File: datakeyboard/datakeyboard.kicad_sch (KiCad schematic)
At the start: 22 parts, among them U1 PIC24FJ128GB204

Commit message: Power supply
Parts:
- removed C?: 100nF, symbol Device:C_Small
- removed R?: R_Small, symbol Device:R_Small
- removed R?: 100, symbol Device:R_Small
- removed U?: FS8205A, symbol Library:FS8205A
- removed U?: DW01A, symbol Library:DW01A
- added C?: 10uF, symbol Device:C_Small
- added D? (x2): LED, symbol Device:LED
- added F?: 400mA, symbol Device:Fuse
- added J?: Micro_SD_Card, symbol Connector:Micro_SD_Card
- added R? (x2): 1k, symbol Device:R_Small
- U?: value AMS1117-3.3 -> AMS1117-3.0
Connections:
- net B- is gone; now on net GND: JBAT.2 (Pin_2)
- net GND: now also C?.1, C?.2; no longer C?.2
- net RESET: now also R?.2; no longer R?.1
- net VUSB: now also F?.2; no longer C?.1, U?.4 (VCC), U?.8 (CE)
- net at C?.1, R?.2: now also R?.1; no longer R?.2
- net at U?.6 (STDBY): now also R?.2
- net at U?.7 (CHRG): now also R?.2
- net +3.3V renamed +3V0
- net VBAT: no longer names the net of JBAT.1 (Pin_1), U?.3 (VI), U?.5 (BAT)
- net VBAT: now also C?.1
- new net: C?.2, D?.2 (A), D?.2 (A), F?.1, U?.4 (VCC), U?.8 (CE)
- new net: D?.1 (K), R?.1 (x2)
- no-connect marks 7 -> 2
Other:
- note removed: "CHARGING"
- note removed: "PROTECTION"
- moved on the sheet: C?, R?, U?

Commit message: Display light
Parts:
- added JDISP: Conn_01x08, symbol Connector_Generic:Conn_01x08
- added Q? (x2): BSS83P, Package_TO_SOT_SMD:SOT-23, symbol Transistor_FET:BSS83P
- added SW0, SW1, SW2, SW3, SW4, SW5: SW_Push, symbol Switch:SW_Push
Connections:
- net +3V0: now also Q?.2 (S), Q?.2 (S)
- net GND: now also J?.6 (VSS), JDISP.1 (Pin_1), SW0.1, SW1.1, SW2.1, SW3.1, SW4.1, SW5.1
- net VIO: now reaches J?.4 (VDD)
- net VIO: now also JDISP.2 (Pin_2), Q?.3 (D)
- net SCLK: now reaches U1.1 (RB9)
- net SCLK: now also JDISP.3 (Pin_3)
- net RES_D: now reaches U1.11 (RB13)
- net RES_D: now also JDISP.5 (Pin_5)
- net at U1.23 (RB2): now also Q?.1 (G)
- net MOSI: now reaches U1.3 (RC7)
- net MOSI: now also JDISP.4 (Pin_4)
- net BTN0: now reaches U1.32 (RA8)
- net BTN0: now also SW0.2
- net BTN1: now reaches U1.33 (RB4)
- net BTN1: now also SW1.2
- net CS_D: now reaches U1.4 (RC8)
- net CS_D: now also JDISP.7 (Pin_7)
- net RS_D: now reaches U1.5 (PC9)
- net RS_D: now also JDISP.6 (Pin_6)
- new net BNT3: SW3.2
- new net BTN2: SW2.2
- new net BTN4: SW4.2
- new net BTN5: SW5.2
- new net LEDA: JDISP.8 (Pin_8), Q?.3 (D)
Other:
- moved on the sheet: C?, J?

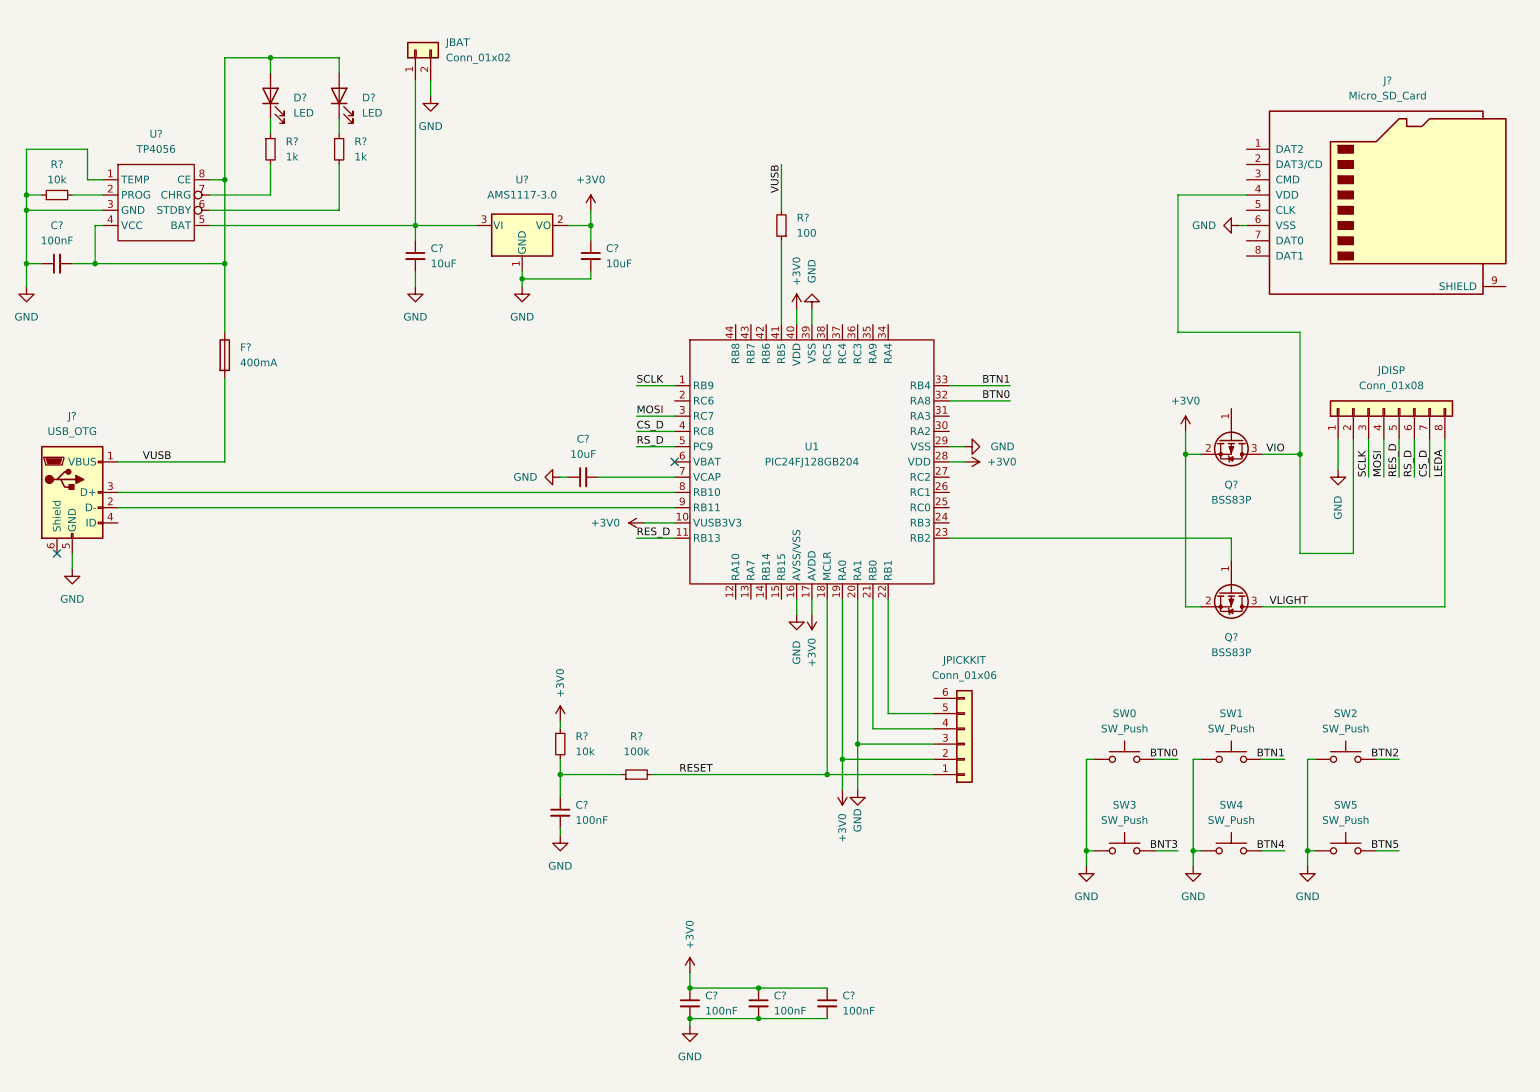
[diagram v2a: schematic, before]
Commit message: Wire up SDCard and buttons
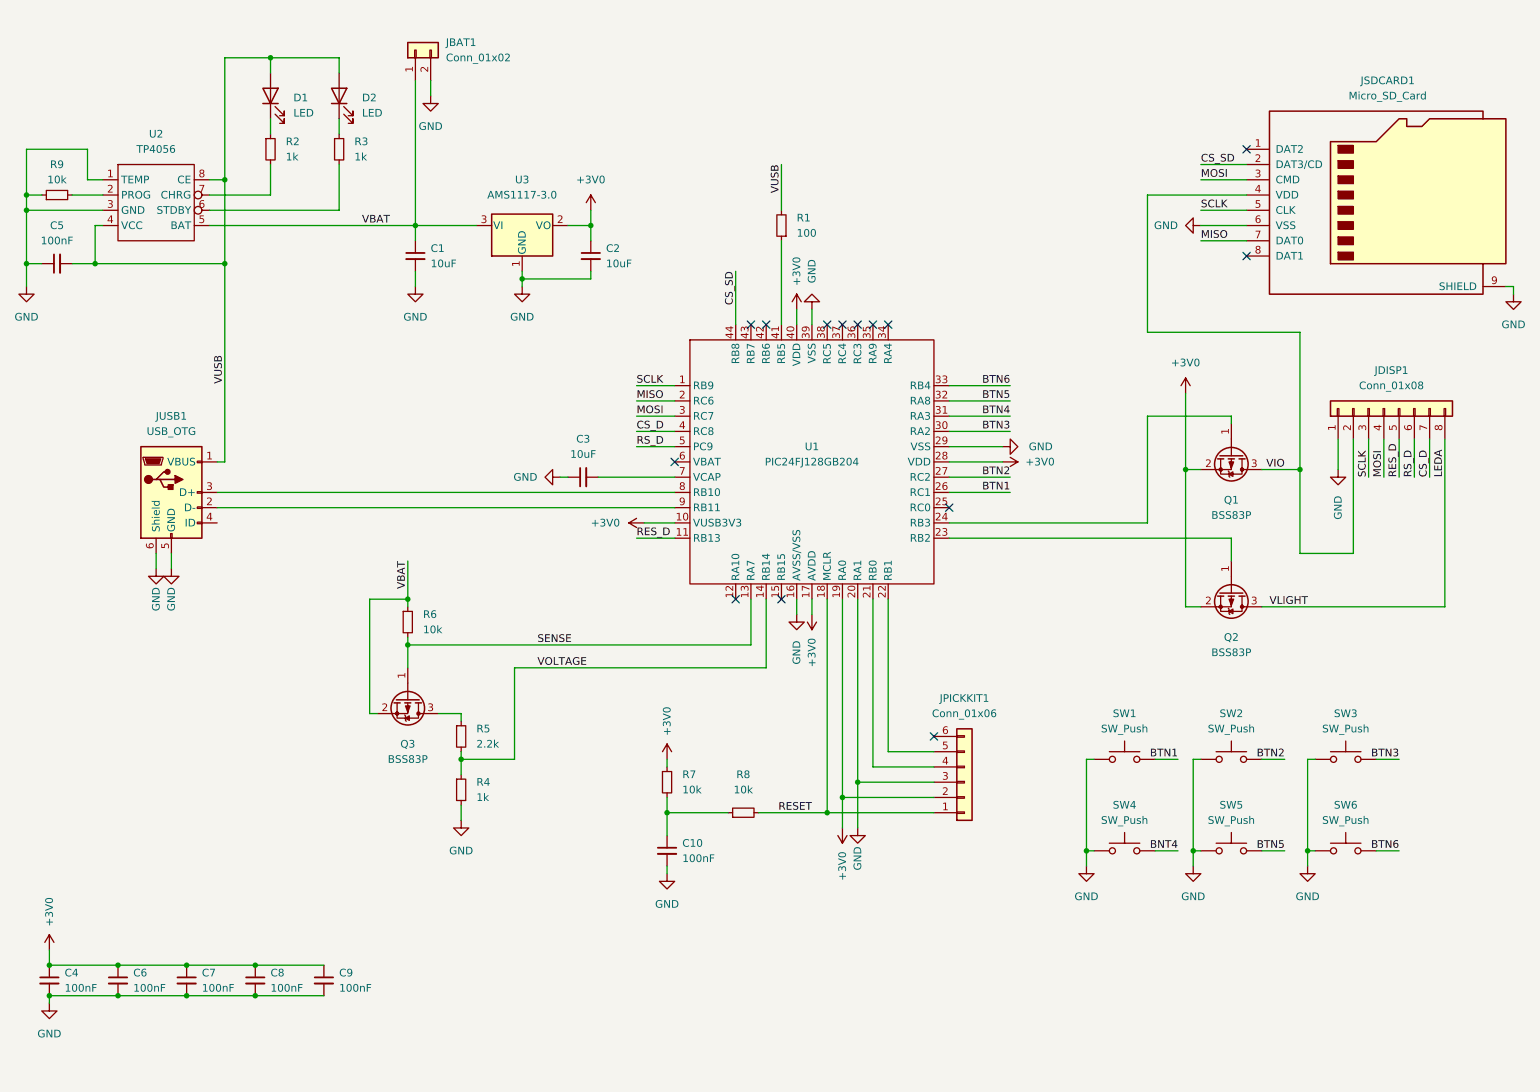
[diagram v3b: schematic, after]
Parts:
- removed F?: 400mA, symbol Device:Fuse
- added C8, C9: 100nF, symbol Device:C_Small
- added Q3: BSS83P, Package_TO_SOT_SMD:SOT-23, symbol Transistor_FET:BSS83P
- added R4: 1k, symbol Device:R_Small
- added R5: 2.2k, symbol Device:R_Small
- added R6: 10k, symbol Device:R_Small
- R8: renamed from R?; value 100k -> 10k
- gave numbers to parts that had none: 21
- renumbered JBAT to JBAT1, JDISP to JDISP1, JPICKKIT to JPICKKIT1, SW0 to SW1, SW1 to SW2, SW2 to SW3, SW3 to SW4, SW4 to SW5, SW5 to SW6
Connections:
- net +3V0: now also C8.1, C9.1
- net BTN1: now also SW1.2, U1.26 (RC1); no longer SW2.2, U1.33 (RB4)
- net BTN2: now also SW2.2, U1.27 (RC2); no longer SW3.2
- net BTN4: now also U1.31 (RA3); no longer SW5.2
- net BTN5: now also SW5.2, U1.32 (RA8); no longer SW6.2
- net GND: now also JSDCARD1.9 (SHIELD), JUSB1.6 (Shield), C8.2, C9.2, R4.2
- net MOSI: now also JSDCARD1.3 (CMD)
- net SCLK: now also JSDCARD1.5 (CLK)
- net VUSB: now also C5.2, D1.2 (A), D2.2 (A), U2.4 (VCC), U2.8 (CE)
- net at Q1.1 (G): now also U1.24 (RB3)
- net CS_SD: now reaches JSDCARD1.2 (DAT3/CD)
- net CS_SD: now also U1.44 (RB8)
- net MISO: now reaches JSDCARD1.7 (DAT0)
- net MISO: now also U1.2 (RC6)
- net VBAT: now reaches C1.1, JBAT1.1 (Pin_1), U2.5 (BAT), U3.3 (VI)
- net VBAT: now also Q3.2 (S), R6.1
- net SENSE: now reaches U1.13 (RA7)
- net SENSE: now also Q3.1 (G), R6.2
- net VOLTAGE: now reaches U1.14 (RB14)
- net VOLTAGE: now also R4.1, R5.2
- net BTN3: now reaches U1.30 (RA2)
- net BTN3: now also SW3.2
- net BNT3 renamed BNT4
- removed net BTN0: SW1.2, U1.32 (RA8)
- new net: Q3.3 (D), R5.1
- new net BTN6: SW6.2, U1.33 (RB4)
- no-connect marks 2 -> 14
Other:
- moved on the sheet: C10, C4, C6, C7, JPICKKIT1, JUSB1, Q1, R7, R8

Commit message: Continue schematics
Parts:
- removed JSDCARD1: Micro_SD_Card, symbol Connector:Micro_SD_Card
- removed U3: AMS1117-3.0, Package_TO_SOT_SMD:SOT-223-3_TabPin2, symbol Regulator_Linear:AMS1117-3.3
- added JCARD1: Micro_SD_Card_Det, symbol Connector:Micro_SD_Card_Det
- added U3: MIC5501-30, Package_TO_SOT_SMD:SOT-23-5, symbol Regulator_Linear:AP131-30
- R8: value 10k -> 100k
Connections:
- net +3V0: now also U3.5 (OUT)
- net BTN1: now also U1.25 (RC0); no longer U1.26 (RC1)
- net BTN2: now also U1.26 (RC1); no longer U1.27 (RC2)
- net BTN3: now also U1.27 (RC2); no longer U1.30 (RA2)
- net BTN4: now also U1.30 (RA2); no longer U1.31 (RA3)
- net BTN6: now also U1.35 (RA9); no longer U1.33 (RB4)
- net CS_SD: now also JCARD1.2 (DAT3/CD)
- net GND: now also JCARD1.11 (SHIELD), JCARD1.6 (VSS), U3.2 (GND)
- net MISO: now also JCARD1.7 (DAT0)
- net MOSI: now also JCARD1.3 (CMD)
- net SCLK: now also JCARD1.5 (CLK)
- net VBAT: now also U3.1 (IN), U3.3 (EN)
- net VIO: now also JCARD1.4 (VDD)
- net at U1.41 (RB5): no longer R1.1
- net at U1.42 (RB6): now also R1.1
- net SENSE_SD: now reaches U1.43 (RB7)
- net SENSE_SD: now also JCARD1.10 (DET_A)
- no-connect marks 14 -> 15
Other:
- moved on the sheet: R1

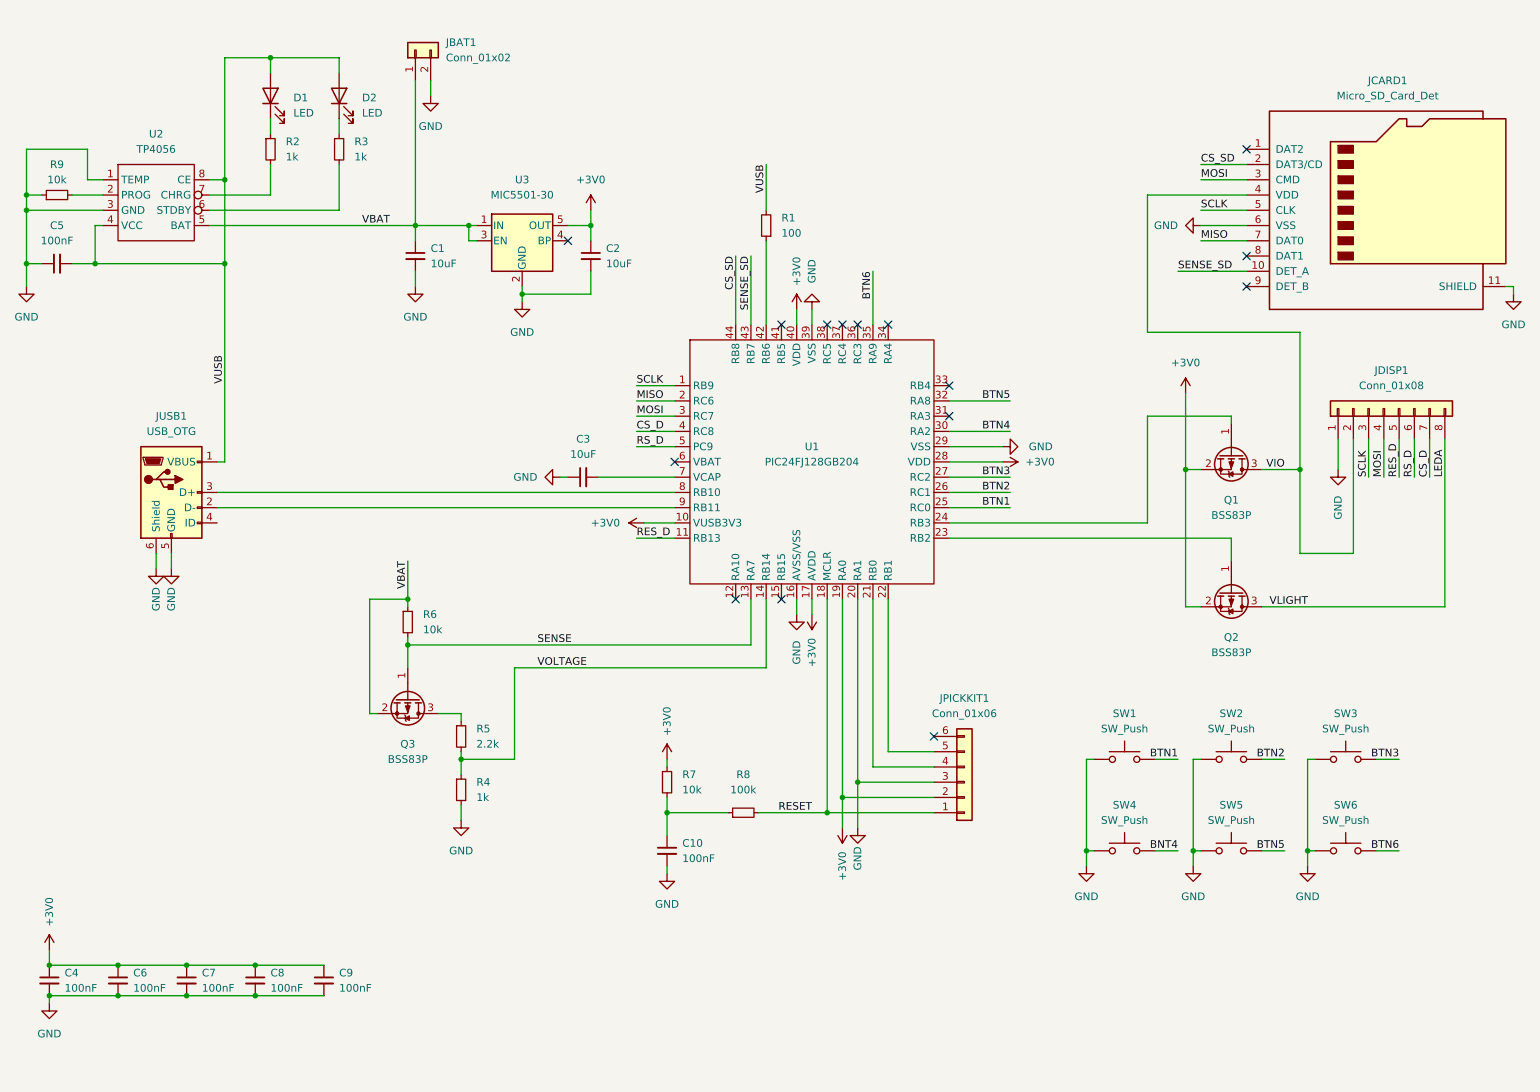
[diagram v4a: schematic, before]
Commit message: Adjust schematics to code
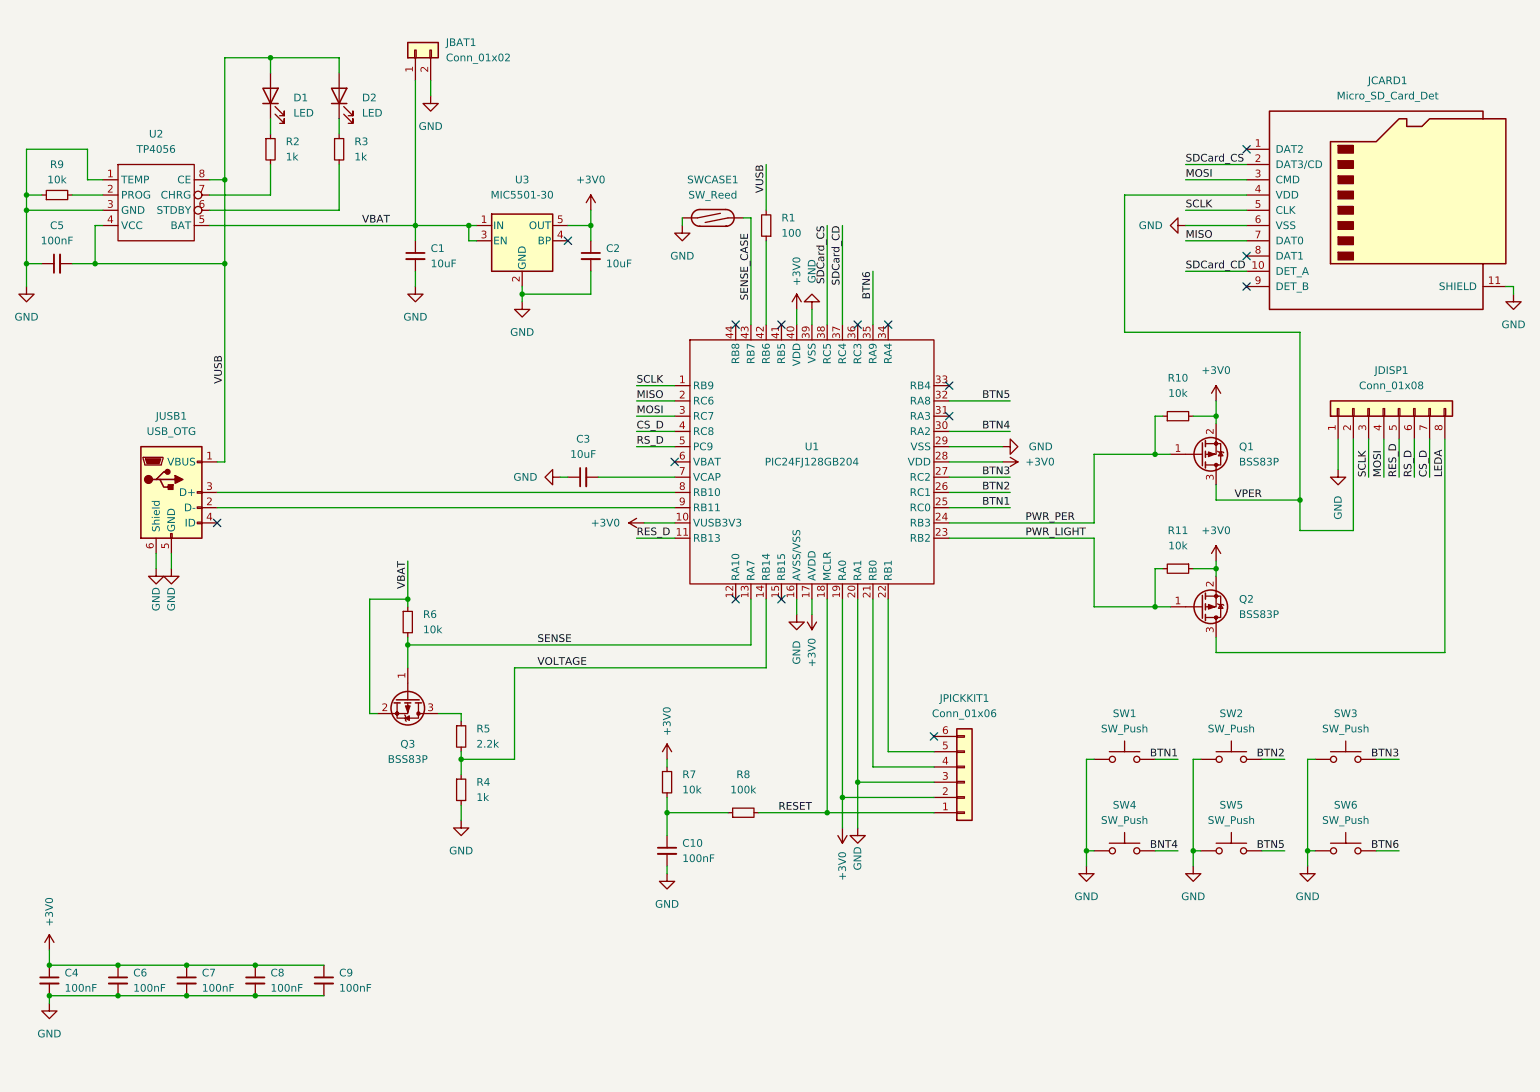
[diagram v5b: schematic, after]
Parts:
- added R10, R11: 10k, symbol Device:R_Small
- added SWCASE1: SW_Reed, symbol Switch:SW_Reed
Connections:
- net +3V0: now also R10.2, R11.1
- net GND: now also SWCASE1.1
- net PWR_PER: now reaches Q1.1 (G), U1.24 (RB3)
- net PWR_PER: now also R10.1
- net PWR_LIGHT: now reaches Q2.1 (G), U1.23 (RB2)
- net PWR_LIGHT: now also R11.2
- net SDCard_CD: now reaches U1.37 (RC4)
- net SDCard_CD: now also JCARD1.10 (DET_A)
- net SDCard_CS: now reaches U1.38 (RC5)
- net SDCard_CS: now also JCARD1.2 (DAT3/CD)
- net CS_SD: no longer names the net of U1.44 (RB8)
- net CS_SD: no longer JCARD1.2 (DAT3/CD)
- net SENSE_SD renamed SENSE_CASE
- net SENSE_CASE: now also SWCASE1.2; no longer JCARD1.10 (DET_A)
- net VIO renamed VPER
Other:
- moved on the sheet: Q1, Q2
